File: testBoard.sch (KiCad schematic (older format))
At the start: 53 parts, among them J1 Conn_01x09, J2 Conn_01x06_Male, Q1 SCT2450KE, U10 INA233, U11 INA233, U12 TPS2557, U13 EMCO_Q50-5, U14 TPS2557, U15 EMCO_Q50-5, U3 WPMDM1500602_171050601, U4 WPMDM1500602_171050601, U5 MAX5483, U6 EMCO_Q10-5, U7 INA233, U8 INA233, U9 INA233

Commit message: Started re-adding symbols
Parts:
- removed CD1-CD12, CIN2, COUT2, CSPK1, CSPK2, Cin1 (x2), Cout1 (x2): C, symbol Device:C
- removed DICSP: D, symbol Device:D
- removed J1: Conn_01x09, symbol Connector_Generic:Conn_01x09
- removed J2: Conn_01x06_Male, symbol Connector:Conn_01x06_Male
- removed Q1: SCT2450KE, symbol Regulator_Switching:SCT2450KE
- removed RAL1, RAL2: R, symbol testBoard-rescue:R-testBoard-rescue
- removed RAL3, RAL4, RAL5, RDB, RDD, RDG, RDT, RF1, RF2, RFBB1 (x2), RFBB2, RFBT1 (x2), RILIM1, RILIM2, RIS1, RIS2, RIS3, RIS4, RIS5, RMCLR: R, symbol Device:R
- removed SW?: SW_Push, symbol Switch:SW_Push
- removed U10, U11, U7, U8, U9: INA233, symbol Amplifier_Current:INA233
- removed U12, U14: TPS2557, symbol Power_Protection:TPS2557
- removed U13, U15: EMCO_Q50-5, symbol Power_Management:EMCO_Q50-5
- removed U3 (x2), U4: WPMDM1500602_171050601, symbol Regulator_Switching:WPMDM1500602_171050601
- removed U5: MAX5483, symbol Potentiometer_Digital:MAX5483
- removed U6: EMCO_Q10-5, symbol Power_Management:EMCO_Q10-5
- removed U?: MAX6816, Package_TO_SOT_SMD:SOT-143, symbol Interface:MAX6816
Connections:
- net labels removed: +5V, GND, PIC_PIN_15, PIC_PIN_16, PIC_PIN_17, PIC_PIN_18, PIC_PIN_19, PIC_PIN_2, PIC_PIN_20, PIC_PIN_23, PIC_PIN_3, PIC_PIN_39, PIC_PIN_4, PIC_PIN_40, PIC_PIN_41, PIC_PIN_5, PIC_Pin_11, SCL, SDA, VBUS_POWER
- wire segments 329 -> 0
- no-connect marks 6 -> 0
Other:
- note removed: "BUS_GND"
- note removed: "SCL_MASTER"
- note removed: "SDA_MASTER"
- note removed: "VBUS"

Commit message: started circuit design
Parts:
- added DISCP: DIODE, symbol pspice:DIODE
- added J2: Conn_01x06, symbol Connector_Generic:Conn_01x06
- added RMCLR, RSCL1, RSDA2: R_US, symbol Device:R_US
- added SW?: SW_Push, symbol Switch:SW_Push
- added U1: PIC18F47K40, symbol PPTBoard-Custom-Parts:PIC18F47K40
- added U?: MAX6816, symbol PPTBoard-Custom-Parts:MAX6816
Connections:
- new net: J2.5 (Pin_5), U1.16 (ICSPCLK/RB6)
- new net: J2.4 (Pin_4), U1.17 (ICSPDAT/RB7)
- new net: DISCP.2 (A), J2.1 (Pin_1), U1.18 (VPP/MCLR/RE3)
- new net: U1.28 (VDD), U1.7 (VDD)
- new net: U1.29 (VSS), U1.6 (VSS), U1.BOTTOM_PAD (VSS)
- new net: SW?.2, U?.2 (IN)
- new net: DISCP.1 (K), RMCLR.1, U?.3 (OUT)
- new net +5V: RMCLR.2, RSCL1.2, RSDA2.2, U?.4 (VCC)
- new net GND: J2.3 (Pin_3), SW?.1, U?.1 (GND)
- new net SCL: RSCL1.1, U1.8 (RB0)
- new net SDA: RSDA2.1, U1.9 (RB1)
- new net U16_CS: U1.24 (RA5)
- new net U17_CS: U1.44 (RC6)
- new net U18_CS: U1.25 (RE0)
- new net VDD: J2.2 (Pin_2)
- no-connect marks 0 -> 1

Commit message: More schematic design
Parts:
- added TC3, TC4, TC5: Thermocouple, symbol Device:Thermocouple
- added U16, U17, U18: MAX6675, symbol PPTBoard-Custom-Parts:MAX6675
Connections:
- net +5V: now also U16.4 (VCC), U17.4 (VCC), U18.4 (VCC)
- net GND: now also U16.1 (GND), U17.1 (GND), U18.1 (GND)
- new net: TC3.2 (-), U16.2 (T-)
- new net: TC3.1 (+), U16.3 (T+)
- new net: TC4.2 (-), U17.2 (T-)
- new net: TC4.1 (+), U17.3 (T+)
- new net: TC5.2 (-), U18.2 (T-)
- new net: TC5.1 (+), U18.3 (T+)
- new net 25: U16.6 (CS)
- new net 26: U17.6 (CS)
- new net 27: U18.6 (CS)
- new net uC_SCK: U16.5 (SCK), U17.5 (SCK), U18.5 (SCK)
- new net uC_SDI: U16.7 (SO), U17.7 (SO), U18.7 (SO)
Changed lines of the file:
@@
 EESchema Schematic File Version 4
+LIBS:testBoard-cache
 EELAYER 26 0
 EELAYER END
-$Descr A4 11693 8268
+$Descr A3 16535 11693
 encoding utf-8
 Sheet 1 1
@@
 	2700 6600 2700 6800
 Connection ~ 2700 6600
+$Comp
+L PPTBoard-Custom-Parts:MAX6675 U16
+U 1 1 5C670EE9
+P 13400 3950
+F 0 "U16" H 13550 4300 50  0000 L CNN
+F 1 "MAX6675" H 12950 4300 50  0000 L CNN
+F 2 "" H 13050 4150 50  0001 C CNN
+F 3 "https://datasheets.maximintegrated.com/en/ds/MAX6675.pdf" H 13050 4150 50  0001 C CNN
+	1    13400 3950
+	1    0    0    -1
+$EndComp
+$Comp
+L power:+5V #PWR?
+U 1 1 5C670FC8
+P 13400 3250
+F 0 "#PWR?" H 13400 3100 50  0001 C CNN
+F 1 "+5V" H 13415 3423 50  0000 C CNN
+F 2 "" H 13400 3250 50  0001 C CNN
+F 3 "" H 13400 3250 50  0001 C CNN
+	1    13400 3250
+	1    0    0    -1
+$EndComp
+Wire Wire Line
+	13400 3250 13400 3550
+Wire Wire Line
+	13400 4350 13400 4600
+$Comp
+L power:GND #PWR?
+U 1 1 5C671EE5
+P 13400 4600
+F 0 "#PWR?" H 13400 4350 50  0001 C CNN
+F 1 "GND" H 13405 4427 50  0000 C CNN
+F 2 "" H 13400 4600 50  0001 C CNN
+F 3 "" H 13400 4600 50  0001 C CNN
+	1    13400 4600
+	1    0    0    -1
+$EndComp
+Text Label 12550 4050 0    50   ~ 0
+uC_SCK
+Wire Wire Line
+	12550 4050 13000 4050
+Wire Wire Line
+	13800 3950 14300 3950
+Text Label 14300 3950 2    50   ~ 0
+uC_SDI
+Wire Wire Line
+	13000 4150 12550 4150
+Text Label 12550 4150 0    50   ~ 0
+25
+$Comp
+L Device:Thermocouple TC3
+U 1 1 5C67427E
+P 12250 3750
+F 0 "TC3" H 12052 3727 50  0000 R CNN
+F 1 "Thermocouple" H 12052 3818 50  0000 R CNN
+F 2 "" H 11675 3800 50  0001 C CNN
+F 3 "~" H 11675 3800 50  0001 C CNN
+	1    12250 3750
+	1    0    0    1
+$EndComp
+Wire Wire Line
+	12350 3650 12700 3650
+Wire Wire Line
+	12700 3650 12700 3750
+Wire Wire Line
+	12700 3750 13000 3750
+Wire Wire Line
+	13000 3850 12350 3850
+$Comp
+L PPTBoard-Custom-Parts:MAX6675 U17
+U 1 1 5C6761CB
+P 13400 5950
+F 0 "U17" H 13550 6300 50  0000 L CNN
+F 1 "MAX6675" H 12950 6300 50  0000 L CNN
+F 2 "" H 13050 6150 50  0001 C CNN
+F 3 "https://datasheets.maximintegrated.com/en/ds/MAX6675.pdf" H 13050 6150 50  0001 C CNN
+	1    13400 5950
+	1    0    0    -1
+$EndComp
+$Comp
+L power:+5V #PWR?
+U 1 1 5C6761D2
+P 13400 5250
+F 0 "#PWR?" H 13400 5100 50  0001 C CNN
+F 1 "+5V" H 13415 5423 50  0000 C CNN
+F 2 "" H 13400 5250 50  0001 C CNN
+F 3 "" H 13400 5250 50  0001 C CNN
+	1    13400 5250
+	1    0    0    -1
+$EndComp
+Wire Wire Line
+	13400 5250 13400 5550
+Wire Wire Line
+	13400 6350 13400 6600
+$Comp
+L power:GND #PWR?
+U 1 1 5C6761DA
+P 13400 6600
+F 0 "#PWR?" H 13400 6350 50  0001 C CNN
+F 1 "GND" H 13405 6427 50  0000 C CNN
+F 2 "" H 13400 6600 50  0001 C CNN
+F 3 "" H 13400 6600 50  0001 C CNN
+	1    13400 6600
+	1    0    0    -1
+$EndComp
+Text Label 12550 6050 0    50   ~ 0
+uC_SCK
+Wire Wire Line
+	12550 6050 13000 6050
+Wire Wire Line
+	13800 5950 14300 5950
+Text Label 14300 5950 2    50   ~ 0
+uC_SDI
+Wire Wire Line
+	13000 6150 12550 6150
+Text Label 12550 6150 0    50   ~ 0
+26
+$Comp
+L Device:Thermocouple TC4
+U 1 1 5C6761E6
+P 12250 5750
+F 0 "TC4" H 12052 5727 50  0000 R CNN
+F 1 "Thermocouple" H 12052 5818 50  0000 R CNN
+F 2 "" H 11675 5800 50  0001 C CNN
+F 3 "~" H 11675 5800 50  0001 C CNN
+	1    12250 5750
+	1    0    0    1
+$EndComp
+Wire Wire Line
+	12350 5650 12700 5650
+Wire Wire Line
+	12700 5650 12700 5750
+Wire Wire Line
+	12700 5750 13000 5750
+Wire Wire Line
+	13000 5850 12350 5850
+$Comp
+L PPTBoard-Custom-Parts:MAX6675 U18
+U 1 1 5C678CAA
+P 13350 8350
+F 0 "U18" H 13500 8700 50  0000 L CNN
+F 1 "MAX6675" H 12900 8700 50  0000 L CNN
+F 2 "" H 13000 8550 50  0001 C CNN
+F 3 "https://datasheets.maximintegrated.com/en/ds/MAX6675.pdf" H 13000 8550 50  0001 C CNN
+	1    13350 8350
+	1    0    0    -1
+$EndComp
+$Comp
+L power:+5V #PWR?
+U 1 1 5C678CB1
+P 13350 7650
+F 0 "#PWR?" H 13350 7500 50  0001 C CNN
+F 1 "+5V" H 13365 7823 50  0000 C CNN
+F 2 "" H 13350 7650 50  0001 C CNN
+F 3 "" H 13350 7650 50  0001 C CNN
+	1    13350 7650
+	1    0    0    -1
+$EndComp
+Wire Wire Line
+	13350 7650 13350 7950
+Wire Wire Line
+	13350 8750 13350 9000
+$Comp
+L power:GND #PWR?
+U 1 1 5C678CB9
+P 13350 9000
+F 0 "#PWR?" H 13350 8750 50  0001 C CNN
+F 1 "GND" H 13355 8827 50  0000 C CNN
+F 2 "" H 13350 9000 50  0001 C CNN
+F 3 "" H 13350 9000 50  0001 C CNN
+	1    13350 9000
+	1    0    0    -1
+$EndComp
+Text Label 12500 8450 0    50   ~ 0
+uC_SCK
+Wire Wire Line
+	12500 8450 12950 8450
+Wire Wire Line
+	13750 8350 14250 8350
+Text Label 14250 8350 2    50   ~ 0
+uC_SDI
+Wire Wire Line
+	12950 8550 12500 8550
+Text Label 12500 8550 0    50   ~ 0
+27
+$Comp
+L Device:Thermocouple TC5
+U 1 1 5C678CC5
+P 12200 8150
+F 0 "TC5" H 12002 8127 50  0000 R CNN
+F 1 "Thermocouple" H 12002 8218 50  0000 R CNN
+F 2 "" H 11625 8200 50  0001 C CNN
+F 3 "~" H 11625 8200 50  0001 C CNN
+	1    12200 8150
+	1    0    0    1
+$EndComp
+Wire Wire Line
+	12300 8050 12650 8050
+Wire Wire Line
+	12650 8050 12650 8150
+Wire Wire Line
+	12650 8150 12950 8150
+Wire Wire Line
+	12950 8250 12300 8250
 $EndSCHEMATC

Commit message: Finished New Schematic of test board
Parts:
- removed DISCP: DIODE, symbol pspice:DIODE
- removed RMCLR, RSCL1, RSDA2: R_US, symbol Device:R_US
- removed SW?: SW_Push, symbol Switch:SW_Push
- removed TC3, TC4, TC5: Thermocouple, symbol Device:Thermocouple
- removed U17, U18: MAX6675, symbol PPTBoard-Custom-Parts:MAX6675
- removed U?: MAX6816, symbol PPTBoard-Custom-Parts:MAX6816
- added CBANK1, CBANK10, CBANK11, CBANK12, CBANK2, CBANK3, CBANK4, CBANK5, CBANK6, CBANK7, CBANK8, CBANK9, CIN1, CIN2, COUT1, COUT2, CSPK1, CSPK2: C, symbol Device:C
- added D1: LED_ALT, symbol Device:LED_ALT
- added D2: LED_RDY, symbol Device:LED_ALT
- added D3, D5: LED_DIA, symbol Device:LED_ALT
- added D4: LED_ERR, symbol Device:LED_ALT
- added DISCP1: DIODE, symbol pspice:DIODE
- added J1: Conn_02x05_Odd_Even, symbol Connector_Generic:Conn_02x05_Odd_Even
- added J3: Conn_01x02, symbol Connector_Generic:Conn_01x02
- added Q1: Conn_01x03, symbol Connector_Generic:Conn_01x03
- added RAL1, RAL2, RAL3, RAL4, RAL5, RBFT1, RDB1, RDT1, RF1, RF2, RFBB1, RFBB2, RILIM1, RILIM2, RIS1, RIS2, RIS3, RIS4, RIS5, RLED1, RLED2, RLED3, RLED4, RLED5, RMCLR1, RSCL1, RSCL2, RSDA1, RSDA2: R, symbol Device:R
- added SW1: PTS645SM43SMTR92_LFS, digikey-footprints:Switch_Tactile_SMD_6x6mm_PTS645, symbol dk_Tactile-Switches:PTS645SM43SMTR92_LFS
- added TC1: Thermocouple, symbol Device:Thermocouple
- added U10, U11, U7, U8, U9: INA233, symbol PPTBoard-Custom-Parts:INA233
- added U12, U14: TPS2557, symbol PPTBoard-Custom-Parts:TPS2557
- added U13, U15: EMCO-Q50-5, symbol PPTBoard-Custom-Parts:EMCO-Q50-5
- added U2: MAX6816, symbol PPTBoard-Custom-Parts:MAX6816
- added U3, U4: WPMDM171050601, symbol PPTBoard-Custom-Parts:WPMDM171050601
- added U5: MAX5483, symbol PPTBoard-Custom-Parts:MAX5483
- added U6: EMCO-Q10-5, symbol PPTBoard-Custom-Parts:EMCO-Q10-5
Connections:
- net +5V is gone; now on net VCC: U16.4 (VCC)
- net 25 is gone; now on net U16_CS: U16.6 (CS)
- net U17_CS is gone; now on net U16_CS: U1.44 (RC6)
- net VDD is gone; now on net VCC: J2.2 (Pin_2)
- net uC_SCK is gone; now on net SCLK: U16.5 (SCK)
- net uC_SDI is gone; now on net U7_SD: U16.7 (SO)
- net GND: now also U1.29 (VSS), U1.6 (VSS), U1.BOTTOM_PAD (VSS), CBANK1.2, CBANK10.2, CBANK11.2, CBANK12.2, CBANK2.2, CBANK3.2, CBANK4.2, CBANK5.2, CBANK6.2, CBANK7.2, CBANK8.2, CBANK9.2, CIN1.1, CIN2.1, COUT1.2, COUT2.2, CSPK1.2, CSPK2.2, J1.10 (Pin_10), J1.9 (Pin_9), Q1.3 (Pin_3), RDB1.1, RFBB1.2, RFBB2.2, RILIM1.2, RILIM2.2, RLED1.1, RLED2.1, RLED3.1, RLED4.1, RLED5.1, SW1.2, U10.1 (A1), U10.7 (GND), U11.2 (A0), U11.7 (GND), U12.1 (GND), U12.POWERPAD (GND), U13.1 ((-)IN), U13.4 (HV_RETURN), U14.1 (GND), U14.POWERPAD (GND), U15.1 ((-)IN), U15.4 (HV_RETURN), U2.1 (GND), U3.2 (SYNC), U3.4 (AGND), U3.EP (AGND), U4.2 (SYNC), U4.4 (AGND), U4.EP (AGND), U5.14 (VSS), U5.2 (GND), U6.1 ((-)IN), U6.4 (HV_RETURN), U7.1 (A1), U7.2 (A0), U7.7 (GND), U8.1 (A1), U8.7 (GND), U9.1 (A1), U9.7 (GND)
- net U16_CS: no longer U1.24 (RA5)
- net SDA2: now reaches U1.10 (RB2)
- net SDA2: now also RSDA2.2, U10.4 (SDA), U11.4 (SDA), U7.4 (SDA), U8.4 (SDA), U9.2 (A0), U9.4 (SDA)
- net U7_ALERT: now reaches U1.11 (RB3)
- net U7_ALERT: now also RAL1.1, U7.3 (ALERT)
- net U8_ALERT: now reaches U1.14 (RB4)
- net U8_ALERT: now also RAL2.1, U8.3 (ALERT)
- net U9_ALERT: now reaches U1.15 (RB5)
- net U9_ALERT: now also RAL3.1, U9.3 (ALERT)
- net ICSPCLK: now reaches J2.5 (Pin_5), U1.16 (ICSPCLK/RB6)
- net ICSPDAT: now reaches J2.4 (Pin_4), U1.17 (ICSPDAT/RB7)
- net MCLR: now reaches J2.1 (Pin_1), U1.18 (VPP/MCLR/RE3)
- net MCLR: now also DISCP1.2 (A)
- net U4_EN: now reaches U1.19 (RA0)
- net U4_EN: now also U4.3 (EN)
- net U12_EN: now reaches U1.2 (RD4)
- net U12_EN: now also U12.4 (EN)
- net at U1.20 (RA1): now also D2.2 (A)
- net at U1.21 (RA2): now also D4.2 (A)
- net at U1.22 (RA3): now also D5.2 (A)
- net RE2: now reaches U1.27 (RE2)
- net RE2: now also RDB1.2, RDT1.1
- net VCC: now reaches U1.28 (VDD), U1.7 (VDD)
- net VCC: now also COUT1.1, D1.2 (A), RAL1.2, RAL2.2, RAL3.2, RAL4.1, RAL5.1, RF1.1, RF2.2, RIS2.2, RMCLR1.1, RSCL1.1, RSCL2.1, RSDA1.1, RSDA2.1, U10.6 (VS), U11.1 (A1), U11.6 (VS), U12.2 (IN), U12.3 (IN), U14.2 (IN), U14.3 (IN), U2.4 (VCC), U5.1 (VDD), U5.6 (SPI(UD)), U7.6 (VS), U8.2 (A0), U8.6 (VS), U8.8 (VBUS), U8.9 (IN-), U9.6 (VS)
- net U14_EN: now reaches U1.3 (RD5)
- net U14_EN: now also U14.4 (EN)
- net at U1.32 (RC0): now also D3.2 (A)
- net U10_ALERT: now reaches U1.36 (RC2)
- net U10_ALERT: now also RAL4.2, U10.3 (ALERT)
- net SCL1: now reaches U1.37 (RC3)
- net SCL1: now also J1.3 (Pin_3), RSCL1.2
- net U7_SD: now reaches U1.38 (RD0)
- net U5_DIN: now reaches U1.39 (RD1)
- net U5_DIN: now also U5.5 (DIN(U/D))
- net U12_FAULT: now reaches U1.4 (RD6)
- net U12_FAULT: now also RF1.2, U12.8 (FAULT)
- net SCLK: now reaches U1.40 (RD2)
- net SCLK: now also U5.4 (SCLK(INC))
- net U5_CS: now reaches U1.41 (RD3)
- net U5_CS: now also U5.3 (CS)
- net SDA1: now reaches U1.42 (RC4)
- net SDA1: now also J1.5 (Pin_5), RSDA1.2
- net U11_ALERT: now reaches U1.43 (RC5)
- net U11_ALERT: now also RAL5.2, U11.3 (ALERT)
- net U14_FAULT: now reaches U1.5 (RD7)
- net U14_FAULT: now also RF2.1, U14.8 (FAULT)
- net at U16.2 (T-): now also TC1.2 (-)
- net at U16.3 (T+): now also TC1.1 (+)
- net SCL: no longer names the net of U1.8 (RB0)
- net SDA renamed SCL2
- net SCL2: now also RSCL2.2, U10.2 (A0), U10.5 (SCL), U11.5 (SCL), U7.5 (SCL), U8.5 (SCL), U9.5 (SCL)
- net U18_CS: no longer names the net of U1.25 (RE0)
- new net: RILIM1.1, U12.5 (ILM)
- new net: RIS4.2, U10.10 (IN+), U12.6 (OUT), U12.7 (OUT)
- new net: RILIM2.1, U14.5 (ILM)
- new net: RIS5.1, U11.10 (IN+), U14.6 (OUT), U14.7 (OUT)
- new net: J1.1 (Pin_1), J1.2 (Pin_2), RIS1.1, U7.10 (IN+)
- new net: RIS3.2, U6.2 ((+)IN), U9.8 (VBUS), U9.9 (IN-)
- new net: DISCP1.1 (K), RMCLR1.2, U2.3 (OUT)
- new net: D3.1 (K), RLED3.2
- new net: D2.1 (K), RLED2.2
- new net: D4.1 (K), RLED4.2
- new net: D5.1 (K), RLED5.2
- new net: J3.1 (Pin_1), Q1.2 (Pin_2)
- new net: RIS5.2, U11.8 (VBUS), U11.9 (IN-), U15.2 ((+)IN)
- new net: CSPK2.1, U15.3 (HV_OUTPUT)
- new net: RFBB2.1, U4.5 (FB), U5.10 (L)
- new net: RIS4.1, U10.8 (VBUS), U10.9 (IN-), U13.2 ((+)IN)
- new net: CSPK1.1, U13.3 (HV_OUTPUT)
- new net: CBANK1.1, CBANK10.1, CBANK11.1, CBANK12.1, CBANK2.1, CBANK3.1, CBANK4.1, CBANK5.1, CBANK6.1, CBANK7.1, CBANK8.1, CBANK9.1, J3.2 (Pin_2), RDT1.2, U6.3 (HV_OUTPUT)
- new net: RBFT1.2, RFBB1.1, U3.5 (FB)
- new net MCLR_BTTN: SW1.4, U2.2 (IN)
- new net PM_VIN: CIN1.2, CIN2.2, RIS1.2, U3.1 (VIN), U4.1 (VIN), U7.8 (VBUS), U7.9 (IN-)
- new net PWR_LED: D1.1 (K), RLED1.2
- new net RA5: Q1.1 (Pin_1), U1.24 (RA5)
- new net U3_VOUT: RBFT1.1, RIS2.1, U3.7 (VOUT), U8.10 (IN+)
- new net U4_VOUT: COUT2.1, RIS3.1, U4.7 (VOUT), U5.11 (W), U9.10 (IN+)
- no-connect marks 1 -> 21
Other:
- note added: "Does not match expressPCB. Suspected \nMistake on expressPCB. Have Dr. White\n double check\n"

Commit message: Added some footprint associations.
Still needs J3, Q1, U15, U6. U13.
U15, U6. U13 need custom made part.
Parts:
- removed CBANK10, CBANK11, CBANK12, CBANK5, CBANK6, CBANK7, CBANK8, CBANK9: C, symbol Device:C
- added CD10, CD11, CD12, CD5, CD6, CD7, CD8, CD9: 0.47u, Capacitor_SMD:C_2220_5650Metric, symbol Device:C
- CD1: renamed from CBANK1; value C -> 0.47u; footprint (none) -> Capacitor_SMD:C_2220_5650Metric
- CD2: renamed from CBANK2; value C -> 0.47u; footprint (none) -> Capacitor_SMD:C_2220_5650Metric
- CD3: renamed from CBANK3; value C -> 0.47u; footprint (none) -> Capacitor_SMD:C_2220_5650Metric
- CD4: renamed from CBANK4; value C -> 0.47u; footprint (none) -> Capacitor_SMD:C_2220_5650Metric
- CIN1, CIN2: value C -> 22u; footprint (none) -> Capacitor_SMD:C_Elec_8x10.2
- COUT1, COUT2: value C -> 330u; footprint (none) -> Capacitor_SMD:C_Elec_6.3x7.7
- CSPK1, CSPK2: value C -> 2200p; footprint (none) -> Capacitor_SMD:C_Elec_6.3x7.7
- D1, D2, D3, D4, D5: footprint (none) -> LED_SMD:LED_1206_3216Metric
- DISCP1: footprint (none) -> Diode_SMD:D_SOD-123
- J1: footprint (none) -> Connector_PinHeader_2.54mm:PinHeader_2x05_P2.54mm_Vertical
- J2: footprint (none) -> Connector_PinHeader_2.54mm:PinHeader_1x06_P2.54mm_Vertical
- RAL1, RAL2, RAL3, RAL4, RAL5, RMCLR1, RSCL1, RSCL2, RSDA1, RSDA2: value R -> 4.7k; footprint (none) -> Resistor_SMD:R_1206_3216Metric
- RDB1: value R -> 500K; footprint (none) -> Resistor_SMD:R_1206_3216Metric
- RDT1: value R -> 100M; footprint (none) -> Resistor_SMD:R_1206_3216Metric
- RF1, RF2, RILIM1, RILIM2: value R -> 100k; footprint (none) -> Resistor_SMD:R_1206_3216Metric
- RFBB1, RFBB2: value R -> 1.87k; footprint (none) -> Resistor_SMD:R_1206_3216Metric
- RFBT1: renamed from RBFT1; value R -> 9.76k; footprint (none) -> Resistor_SMD:R_1206_3216Metric
- RIS1, RIS2, RIS3, RIS4, RIS5: value R -> 0.01; footprint (none) -> Resistor_SMD:R_1206_3216Metric
- RLED1, RLED2, RLED3, RLED4, RLED5: value R -> 100; footprint (none) -> Resistor_SMD:R_1206_3216Metric
- TC1: footprint (none) -> Connector_PinHeader_2.54mm:PinHeader_2x01_P2.54mm_Vertical
- U1: footprint (none) -> Package_QFP:TQFP-44-1EP_10x10mm_P0.8mm_EP4.5x4.5mm
- U10, U11, U7, U8, U9: footprint (none) -> Package_SO:VSSOP-10_3x3mm_P0.5mm
- U12, U14: footprint (none) -> Package_SON:Texas_S-PVSON-N8
- U16: footprint (none) -> Package_SO:SOIC-8_3.9x4.9mm_P1.27mm
- U2: footprint (none) -> Package_TO_SOT_SMD:SOT-143
- U3, U4: footprint (none) -> Package_TO_SOT_SMD:TO-263-7_TabPin8
- U5: footprint (none) -> Package_SO:TSSOP-14_4.4x5mm_P0.65mm
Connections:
- net GND: now also CD10.2, CD11.2, CD12.2, CD5.2, CD6.2, CD7.2, CD8.2, CD9.2
- net at CD1.1, CD2.1, CD3.1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: now also CD10.1, CD11.1, CD12.1, CD5.1, CD6.1, CD7.1, CD8.1, CD9.1

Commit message: Added EMCO DC-DC Converter components
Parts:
- U13, U15, U6: footprint (none) -> PPTBoard:EMCO_Q_2.5-5kV
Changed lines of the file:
@@
 F 0 "U13" H 4950 9217 50  0000 C CNN
 F 1 "EMCO-Q50-5" H 4950 9126 50  0000 C CNN
-F 2 "" H 4350 8950 50  0001 C CNN
+F 2 "PPTBoard:EMCO_Q_2.5-5kV" H 4350 8950 50  0001 C CNN
 F 3 "https://www.xppower.com/Portals/0/pdfs/SF_Q_Series.pdf" H 4350 8950 50  0001 C CNN
 	1    4950 8750
@@
 F 0 "U6" H 2550 7517 50  0000 C CNN
 F 1 "EMCO-Q10-5" H 2550 7426 50  0000 C CNN
-F 2 "" H 1950 7250 50  0001 C CNN
+F 2 "PPTBoard:EMCO_Q_2.5-5kV" H 1950 7250 50  0001 C CNN
 F 3 "https://www.xppower.com/Portals/0/pdfs/SF_Q_Series.pdf" H 1950 7250 50  0001 C CNN
 	1    2550 7050
@@
 F 0 "U15" H 13900 2167 50  0000 C CNN
 F 1 "EMCO-Q50-5" H 13900 2076 50  0000 C CNN
-F 2 "" H 13300 1900 50  0001 C CNN
+F 2 "PPTBoard:EMCO_Q_2.5-5kV" H 13300 1900 50  0001 C CNN
 F 3 "https://www.xppower.com/Portals/0/pdfs/SF_Q_Series.pdf" H 13300 1900 50  0001 C CNN
 	1    13900 1700

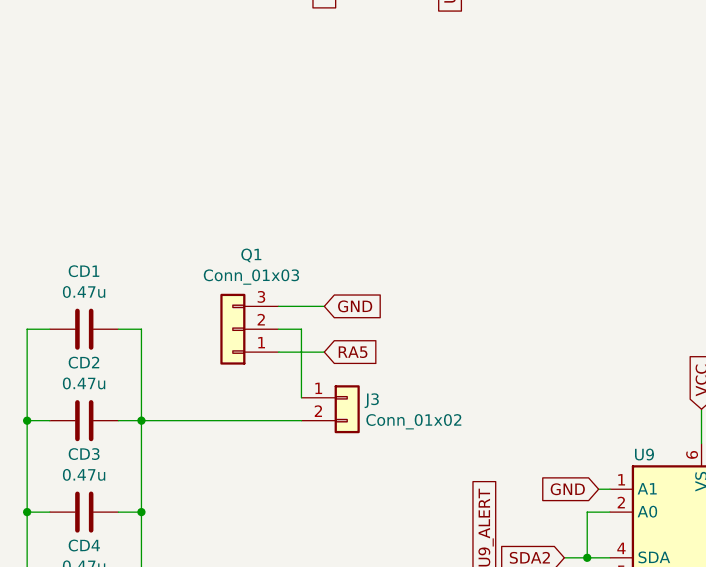
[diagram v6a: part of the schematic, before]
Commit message: Fix MOSFET, Add Wire Header
*Fixed Q1 being a pin header instead of a mosfet.
*Added footprint for the thick wires that attached from board to thruster, and added association to schematic
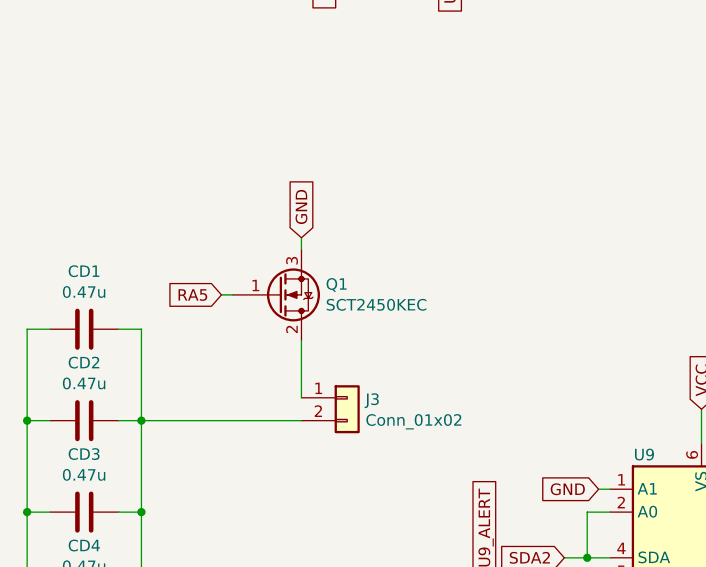
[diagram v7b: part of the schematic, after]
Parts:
- removed Q1: Conn_01x03, symbol Connector_Generic:Conn_01x03
- added Q1: SCT2450KEC, Package_TO_SOT_THT:TO-247-3_Vertical, symbol Device:Q_NMOS_GDS
- J3: footprint (none) -> PPTBoard:SolderWirePad_1x02_P0.220in_Drill0.110in
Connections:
- net GND: now also Q1.3 (S)
- net RA5: now also Q1.1 (G)
- net at J3.1 (Pin_1): now also Q1.2 (D)
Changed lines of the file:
@@
 NoConn ~ 7300 3550
 NoConn ~ 7300 4850
-$Comp
-L Connector_Generic:Conn_01x03 Q1
-U 1 1 5CC2043D
-P 1400 5100
-F 0 "Q1" H 1318 4775 50  0000 C CNN
-F 1 "Conn_01x03" H 1318 4866 50  0000 C CNN
-F 2 "" H 1400 5100 50  0001 C CNN
-F 3 "~" H 1400 5100 50  0001 C CNN
-	1    1400 5100
-	-1   0    0    1
-$EndComp
-Wire Wire Line
-	1600 5000 1800 5000
-Text GLabel 1800 5000 2    50   Input ~ 0
+Text GLabel 1700 4700 1    50   Input ~ 0
 GND
 Wire Wire Line
@@
 Wire Wire Line
 	1950 6700 1950 6850
-Wire Wire Line
-	1700 5100 1600 5100
 Wire Wire Line
 	14700 8100 14700 7850
@@
 PM_VIN
 Wire Wire Line
-	1600 5200 1800 5200
-Wire Wire Line
 	1700 5500 1000 5500
 $Comp
@@
 F 0 "J3" H 1980 5392 50  0000 L CNN
 F 1 "Conn_01x02" H 1980 5301 50  0000 L CNN
-F 2 "" H 1900 5400 50  0001 C CNN
+F 2 "PPTBoard:SolderWirePad_1x02_P0.220in_Drill0.110in" H 1900 5400 50  0001 C CNN
 F 3 "~" H 1900 5400 50  0001 C CNN
 	1    1900 5400
 	1    0    0    -1
 $EndComp
-Wire Wire Line
-	1700 5100 1700 5400
 Wire Wire Line
 	2200 3100 2350 3100
@@
 Text GLabel 7050 3450 0    50   Input ~ 0
 RA5
-Text GLabel 1800 5200 2    50   Input ~ 0
+Text GLabel 1350 4950 0    50   Input ~ 0
 RA5
 Wire Wire Line
@@
 	1    0    0    -1
 $EndComp
+$Comp
+L Device:Q_NMOS_GDS Q1
+U 1 1 5CBCE1A4
+P 1600 4950
+F 0 "Q1" H 1806 4904 50  0000 L CNN
+F 1 "SCT2450KEC" H 1806 4995 50  0000 L CNN
+F 2 "Package_TO_SOT_THT:TO-247-3_Vertical" H 1800 5050 50  0001 C CNN
+F 3 "~" H 1600 4950 50  0001 C CNN
+	1    1600 4950
+	1    0    0    1
+$EndComp
+Wire Wire Line
+	1350 4950 1400 4950
+Wire Wire Line
+	1700 4700 1700 4750
+Wire Wire Line
+	1700 5400 1700 5150
 $EndSCHEMATC
